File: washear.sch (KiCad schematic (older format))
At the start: 32 parts

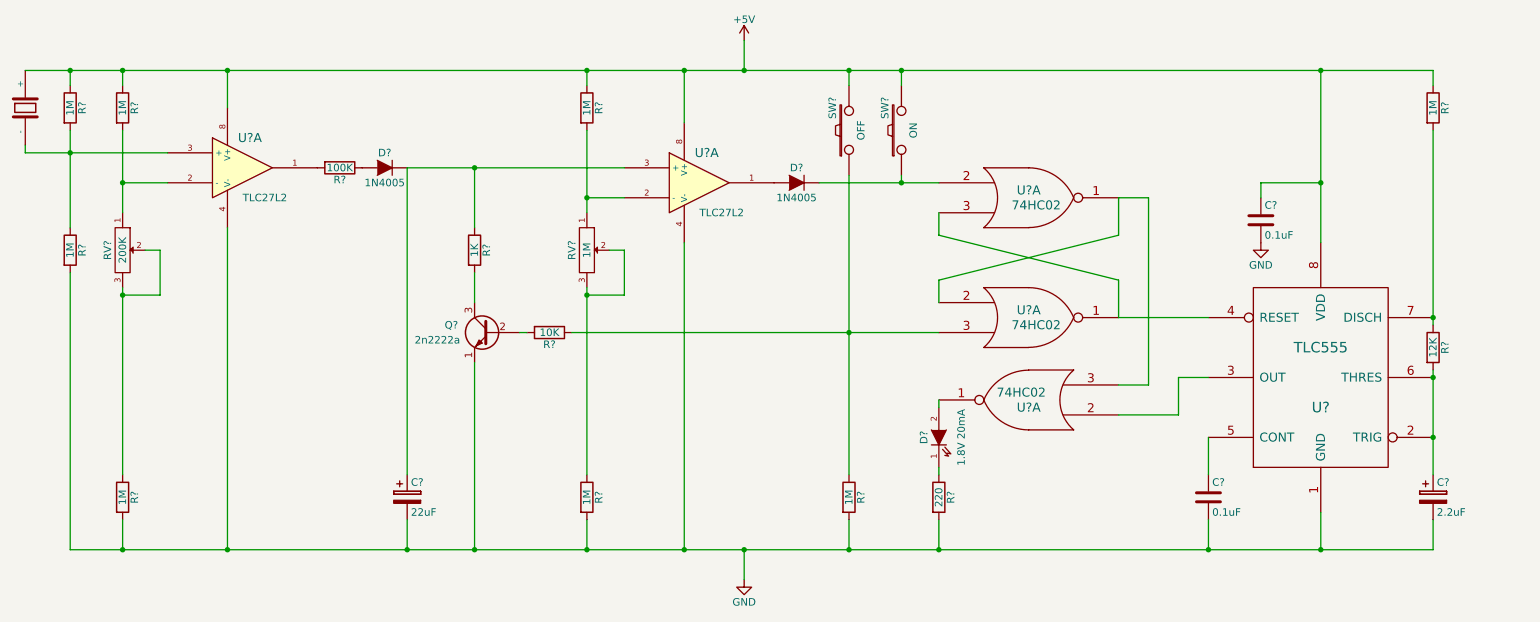
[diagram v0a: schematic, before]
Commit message: Power TLC555 from logic gate to save power
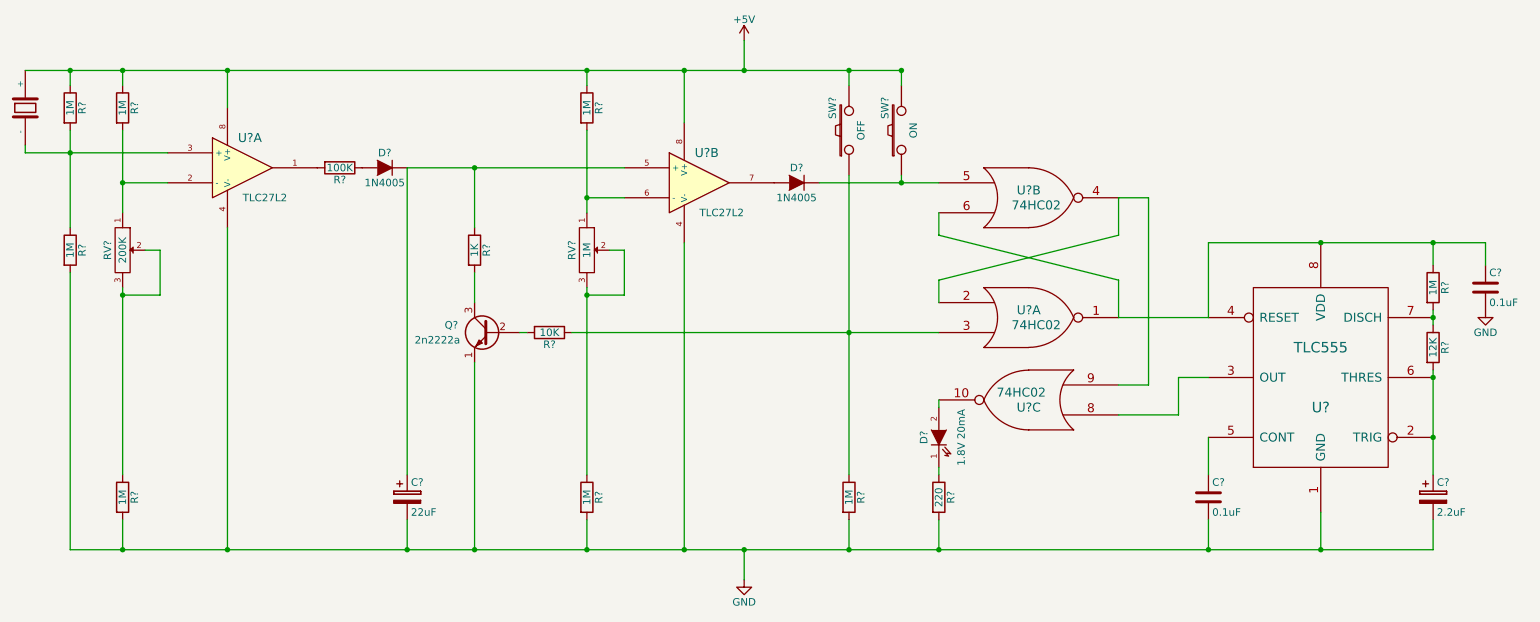
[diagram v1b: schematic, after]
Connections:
- net +5V: no longer C?.1, R?.1, U?.8 (VDD)
- net at U?.1, U?.4 (RESET): now also C?.1, R?.1, U?.6, U?.8 (VDD); no longer U?.3
- net at D?.1 (K), SW?.1: now also U?.5; no longer U?.2
- net at D?.2 (A): now also U?.7; no longer U?.1
- net at R?.2, RV?.1: now also U?.6 (-); no longer U?.2 (-)
- net at C?.1, D?.1 (K), R?.1: now also U?.5 (+); no longer U?.3 (+)
- net at D?.2 (A): now also U?.10; no longer U?.1
- net at U?.3 (OUT): now also U?.8; no longer U?.2
- new net: U?.2, U?.4, U?.9
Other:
- moved on the sheet: C?, R?
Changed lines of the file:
@@
 $Comp
 L 74HC02 U?
-U 1 1 55D4E108
+U 2 1 55D4E108
 P 7700 3250
 F 0 "U?" H 7700 3300 60  0000 C CNN
@@
 F 2 "~" H 7700 3250 60  0000 C CNN
 F 3 "~" H 7700 3250 60  0000 C CNN
-	1    7700 3250
+	2    7700 3250
 	1    0    0    -1
 $EndComp
@@
 $Comp
 L TLC27L2 U?
-U 1 1 55E35DBE
+U 2 1 55E35DBE
 P 5500 3150
 F 0 "U?" H 5550 3350 60  0000 C CNN
@@
 F 2 "" H 5500 3150 60  0000 C CNN
 F 3 "" H 5500 3150 60  0000 C CNN
-	1    5500 3150
+	2    5500 3150
 	1    0    0    -1
 $EndComp
@@
 Wire Wire Line
 	8300 3500 8300 3250
-Wire Wire Line
-	1000 2400 1300 2400
-Wire Wire Line
-	1300 2400 1650 2400
-Wire Wire Line
-	1650 2400 2350 2400
-Wire Wire Line
-	2350 2400 4750 2400
-Wire Wire Line
-	4750 2400 5400 2400
-Wire Wire Line
-	5400 2400 5800 2400
-Wire Wire Line
-	5800 2400 6500 2400
-Wire Wire Line
-	6500 2400 6850 2400
-Wire Wire Line
-	6850 2400 9650 2400
-Wire Wire Line
-	9650 2400 10400 2400
 Connection ~ 1650 5600
 Wire Wire Line
@@
 	9650 5600 10400 5600
 Connection ~ 8900 5600
-Wire Wire Line
-	9650 2400 9650 3150
-Wire Wire Line
-	9650 3150 9650 3550
 $Comp
 L R R?
 U 1 1 567C5142
-P 10400 2650
-F 0 "R?" V 10480 2650 50  0000 C CNN
-F 1 "1M" V 10400 2650 50  0000 C CNN
-F 2 "" V 10330 2650 30  0000 C CNN
-F 3 "" H 10400 2650 30  0000 C CNN
-	1    10400 2650
-	1    0    0    -1
-$EndComp
-Wire Wire Line
-	10400 2400 10400 2500
-Connection ~ 9650 2400
+P 10400 3850
+F 0 "R?" V 10480 3850 50  0000 C CNN
+F 1 "1M" V 10400 3850 50  0000 C CNN
+F 2 "" V 10330 3850 30  0000 C CNN
+F 3 "" H 10400 3850 30  0000 C CNN
+	1    10400 3850
+	1    0    0    -1
+$EndComp
 $Comp
 L R R?
@@
 $Comp
 L 74HC02 U?
-U 1 1 567C7051
+U 3 1 567C7051
 P 7700 4600
 F 0 "U?" H 7700 4650 60  0000 C CNN
@@
 F 2 "~" H 7700 4600 60  0000 C CNN
 F 3 "~" H 7700 4600 60  0000 C CNN
-	1    7700 4600
+	3    7700 4600
 	-1   0    0    1
 $EndComp
@@
 L C C?
 U 1 1 567ED50A
-P 9250 3400
-F 0 "C?" H 9275 3500 50  0000 L CNN
-F 1 "0.1uF" H 9275 3300 50  0000 L CNN
-F 2 "" H 9288 3250 30  0000 C CNN
-F 3 "" H 9250 3400 60  0000 C CNN
-	1    9250 3400
+P 10750 3850
+F 0 "C?" H 10775 3950 50  0000 L CNN
+F 1 "0.1uF" H 10775 3750 50  0000 L CNN
+F 2 "" H 10788 3700 30  0000 C CNN
+F 3 "" H 10750 3850 60  0000 C CNN
+	1    10750 3850
 	1    0    0    -1
 $EndComp
@@
 L GND #PWR?
 U 1 1 567ED5C0
-P 9250 3550
-F 0 "#PWR?" H 9250 3300 50  0001 C CNN
-F 1 "GND" H 9250 3400 50  0000 C CNN
-F 2 "" H 9250 3550 60  0000 C CNN
-F 3 "" H 9250 3550 60  0000 C CNN
-	1    9250 3550
-	1    0    0    -1
-$EndComp
-Wire Wire Line
-	9250 3150 9250 3250
+P 10750 4000
+F 0 "#PWR?" H 10750 3750 50  0001 C CNN
+F 1 "GND" H 10750 3850 50  0000 C CNN
+F 2 "" H 10750 4000 60  0000 C CNN
+F 3 "" H 10750 4000 60  0000 C CNN
+	1    10750 4000
+	1    0    0    -1
+$EndComp
 $Comp
 L D D?
@@
 	9650 5350 9650 5600
 Wire Wire Line
-	10400 2800 10400 4050
+	10400 4000 10400 4050
 Wire Wire Line
 	10400 4050 10400 4100
@@
 	1    0    0    -1
 $EndComp
-Wire Wire Line
-	9250 3150 9650 3150
-Connection ~ 9650 3150
 $Comp
 L TLC555 U?
@@
 	1    0    0    -1
 $EndComp
+Wire Wire Line
+	8900 4050 8900 3550
+Wire Wire Line
+	8900 3550 9650 3550
+Wire Wire Line
+	9650 3550 10400 3550
+Wire Wire Line
+	10400 3550 10750 3550
+Wire Wire Line
+	10400 3550 10400 3700
+Connection ~ 9650 3550
+Wire Wire Line
+	10750 3550 10750 3700
+Connection ~ 10400 3550
+Wire Wire Line
+	1000 2400 1300 2400
+Wire Wire Line
+	1300 2400 1650 2400
+Wire Wire Line
+	1650 2400 2350 2400
+Wire Wire Line
+	2350 2400 4750 2400
+Wire Wire Line
+	4750 2400 5400 2400
+Wire Wire Line
+	5400 2400 5800 2400
+Wire Wire Line
+	5800 2400 6500 2400
+Wire Wire Line
+	6500 2400 6850 2400
 $EndSCHEMATC

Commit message: Capture the final implemented schematic
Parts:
- RV1: renamed from RV?; value 200K -> 100K
- RV2: renamed from RV?; value 1M -> 500K
- gave numbers to parts that had none: 27
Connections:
- net at C4.1, R12.1, U3.4 (RESET)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: now also U2.3, U2.4; no longer U2.1, U2.6
- net at R10.1, R7.1, SW1.1: now also U2.6; no longer U2.3
- net at D2.1 (K), SW2.1: now also U2.2; no longer U2.5
- net at D3.2 (A): now also U2.13; no longer U2.10
- net at U3.3 (OUT): now also U2.11; no longer U2.8
- new net: U2.1, U2.12, U2.5
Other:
- moved on the sheet: C4
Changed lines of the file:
@@
 $EndDescr
 $Comp
-L PZ PZ?
+L PZ PZ1
 U 1 1 55D47824
 P 1000 2650
-F 0 "PZ?" H 1000 2780 40  0001 L CNN
+F 0 "PZ1" H 1000 2780 40  0001 L CNN
 F 1 "PZ" H 1006 2535 40  0001 L CNN
 F 2 "~" H 1038 2470 30  0000 C CNN
@@
 $EndComp
 $Comp
-L POT RV?
+L POT RV1
 U 1 1 55D4DDDE
 P 1650 3600
-F 0 "RV?" H 1650 3500 50  0000 C CNN
-F 1 "200K" H 1650 3600 50  0000 C CNN
+F 0 "RV1" H 1650 3500 50  0000 C CNN
+F 1 "100K" H 1650 3600 50  0000 C CNN
 F 2 "~" H 1650 3600 60  0000 C CNN
 F 3 "~" H 1650 3600 60  0000 C CNN
@@
 $EndComp
 $Comp
-L 74HC02 U?
-U 1 1 55D4DFF4
+L 74HC02 U2
+U 2 1 55D4DFF4
 P 7700 4050
-F 0 "U?" H 7700 4100 60  0000 C CNN
+F 0 "U2" H 7700 4100 60  0000 C CNN
 F 1 "74HC02" H 7750 4000 60  0000 C CNN
 F 2 "~" H 7700 4050 60  0000 C CNN
 F 3 "~" H 7700 4050 60  0000 C CNN
-	1    7700 4050
-	1    0    0    -1
-$EndComp
-$Comp
-L 74HC02 U?
-U 2 1 55D4E108
+	2    7700 4050
+	1    0    0    -1
+$EndComp
+$Comp
+L 74HC02 U2
+U 1 1 55D4E108
 P 7700 3250
-F 0 "U?" H 7700 3300 60  0000 C CNN
+F 0 "U2" H 7700 3300 60  0000 C CNN
 F 1 "74HC02" H 7750 3200 60  0000 C CNN
 F 2 "~" H 7700 3250 60  0000 C CNN
 F 3 "~" H 7700 3250 60  0000 C CNN
-	2    7700 3250
-	1    0    0    -1
-$EndComp
-$Comp
-L TLC27L2 U?
+	1    7700 3250
+	1    0    0    -1
+$EndComp
+$Comp
+L TLC27L2 U1
 U 1 1 55E34D0D
 P 2450 3050
-F 0 "U?" H 2500 3250 60  0000 C CNN
+F 0 "U1" H 2500 3250 60  0000 C CNN
 F 1 "TLC27L2" H 2600 2850 50  0000 C CNN
 F 2 "" H 2450 3050 60  0000 C CNN
@@
 $EndComp
 $Comp
-L TLC27L2 U?
+L TLC27L2 U1
 U 2 1 55E35DBE
 P 5500 3150
-F 0 "U?" H 5550 3350 60  0000 C CNN
+F 0 "U1" H 5550 3350 60  0000 C CNN
 F 1 "TLC27L2" H 5650 2950 50  0000 C CNN
 F 2 "" H 5500 3150 60  0000 C CNN
@@
 $EndComp
 $Comp
-L POT RV?
+L POT RV2
 U 1 1 55E35EEA
 P 4750 3600
-F 0 "RV?" H 4750 3500 50  0000 C CNN
-F 1 "1M" H 4750 3600 50  0000 C CNN
+F 0 "RV2" H 4750 3500 50  0000 C CNN
+F 1 "500K" H 4750 3600 50  0000 C CNN
 F 2 "~" H 4750 3600 60  0000 C CNN
 F 3 "~" H 4750 3600 60  0000 C CNN
@@
 $EndComp
 $Comp
-L SW_PUSH SW?
+L SW_PUSH SW1
 U 1 1 5627B2CF
 P 6500 2800
-F 0 "SW?" H 6650 2910 50  0000 C CNN
+F 0 "SW1" H 6650 2910 50  0000 C CNN
 F 1 "OFF" H 6500 2720 50  0000 C CNN
 F 2 "~" H 6500 2800 60  0000 C CNN
@@
 $EndComp
 $Comp
-L SW_PUSH SW?
+L SW_PUSH SW2
 U 1 1 5627B2DC
 P 6850 2800
-F 0 "SW?" H 7000 2910 50  0000 C CNN
+F 0 "SW2" H 7000 2910 50  0000 C CNN
 F 1 "ON" H 6850 2720 50  0000 C CNN
 F 2 "~" H 6850 2800 60  0000 C CNN
@@
 	7100 3800 8300 3500
 $Comp
-L C C?
+L C C2
 U 1 1 567C46A0
 P 8900 5250
-F 0 "C?" H 8925 5350 50  0000 L CNN
+F 0 "C2" H 8925 5350 50  0000 L CNN
 F 1 "0.1uF" H 8925 5150 50  0000 L CNN
 F 2 "" H 8938 5100 30  0000 C CNN
@@
 	8900 5600 8900 5400
 $Comp
-L R R?
+L R R13
 U 1 1 567C4B96
 P 10400 4250
-F 0 "R?" V 10480 4250 50  0000 C CNN
+F 0 "R13" V 10480 4250 50  0000 C CNN
 F 1 "12K" V 10400 4250 50  0000 C CNN
 F 2 "" V 10330 4250 30  0000 C CNN
@@
 $EndComp
 $Comp
-L CP C?
+L CP C3
 U 1 1 567C4E2B
 P 10400 5250
-F 0 "C?" H 10425 5350 50  0000 L CNN
+F 0 "C3" H 10425 5350 50  0000 L CNN
 F 1 "2.2uF" H 10425 5150 50  0000 L CNN
 F 2 "" H 10438 5100 30  0000 C CNN
@@
 Wire Wire Line
 	9650 5600 10400 5600
+Wire Wire Line
+	10400 5600 10750 5600
 Connection ~ 8900 5600
 $Comp
-L R R?
+L R R12
 U 1 1 567C5142
 P 10400 3850
-F 0 "R?" V 10480 3850 50  0000 C CNN
+F 0 "R12" V 10480 3850 50  0000 C CNN
 F 1 "1M" V 10400 3850 50  0000 C CNN
 F 2 "" V 10330 3850 30  0000 C CNN
@@
 $EndComp
 $Comp
-L R R?
+L R R8
 U 1 1 567C5369
 P 4750 2650
-F 0 "R?" V 4830 2650 50  0000 C CNN
+F 0 "R8" V 4830 2650 50  0000 C CNN
 F 1 "1M" V 4750 2650 50  0000 C CNN
 F 2 "" V 4680 2650 30  0000 C CNN
@@
 $EndComp
 Wire Wire Line
-	4750 2500 4750 2400
-$Comp
-L R R?
+	4750 2400 4750 2500
+$Comp
+L R R1
 U 1 1 567C567F
 P 1300 2650
-F 0 "R?" V 1380 2650 50  0000 C CNN
+F 0 "R1" V 1380 2650 50  0000 C CNN
 F 1 "1M" V 1300 2650 50  0000 C CNN
 F 2 "" V 1230 2650 30  0000 C CNN
@@
 $EndComp
 $Comp
-L R R?
+L R R3
 U 1 1 567C572F
 P 1650 2650
-F 0 "R?" V 1730 2650 50  0000 C CNN
+F 0 "R3" V 1730 2650 50  0000 C CNN
 F 1 "1M" V 1650 2650 50  0000 C CNN
 F 2 "" V 1580 2650 30  0000 C CNN
@@
 	1650 2400 1650 2500
 $Comp
-L R R?
+L R R2
 U 1 1 567C595D
 P 1300 3600
-F 0 "R?" V 1380 3600 50  0000 C CNN
+F 0 "R2" V 1380 3600 50  0000 C CNN
 F 1 "1M" V 1300 3600 50  0000 C CNN
 F 2 "" V 1230 3600 30  0000 C CNN
@@
 $EndComp
 $Comp
-L R R?
+L R R4
 U 1 1 567C5B76
 P 1650 5250
-F 0 "R?" V 1730 5250 50  0000 C CNN
+F 0 "R4" V 1730 5250 50  0000 C CNN
 F 1 "1M" V 1650 5250 50  0000 C CNN
 F 2 "" V 1580 5250 30  0000 C CNN
@@
 $EndComp
 $Comp
-L R R?
+L R R9
 U 1 1 567C5E2F
 P 4750 5250
-F 0 "R?" V 4830 5250 50  0000 C CNN
+F 0 "R9" V 4830 5250 50  0000 C CNN
 F 1 "1M" V 4750 5250 50  0000 C CNN
 F 2 "" V 4680 5250 30  0000 C CNN
@@
 $EndComp
 $Comp
-L R R?
+L R R10
 U 1 1 567C606F
 P 6500 5250
-F 0 "R?" V 6580 5250 50  0000 C CNN
+F 0 "R10" V 6580 5250 50  0000 C CNN
 F 1 "1M" V 6500 5250 50  0000 C CNN
 F 2 "" V 6430 5250 30  0000 C CNN
@@
 $EndComp
 $Comp
-L CP C?
+L CP C1
 U 1 1 567C65FE
 P 3550 5250
-F 0 "C?" H 3575 5350 50  0000 L CNN
+F 0 "C1" H 3575 5350 50  0000 L CNN
 F 1 "22uF" H 3575 5150 50  0000 L CNN
 F 2 "" H 3588 5100 30  0000 C CNN
@@
 $EndComp
 $Comp
-L R R?
+L R R5
 U 1 1 567C6977
 P 3100 3050
-F 0 "R?" V 3180 3050 50  0000 C CNN
+F 0 "R5" V 3180 3050 50  0000 C CNN
 F 1 "100K" V 3100 3050 50  0000 C CNN
 F 2 "" V 3030 3050 30  0000 C CNN
@@
 $EndComp
 $Comp
-L 74HC02 U?
-U 3 1 567C7051
+L 74HC02 U2
+U 4 1 567C7051
 P 7700 4600
-F 0 "U?" H 7700 4650 60  0000 C CNN
+F 0 "U2" H 7700 4650 60  0000 C CNN
 F 1 "74HC02" H 7750 4550 60  0000 C CNN
 F 2 "~" H 7700 4600 60  0000 C CNN
 F 3 "~" H 7700 4600 60  0000 C CNN
-	3    7700 4600
+	4    7700 4600
 	-1   0    0    1
 $EndComp
 $Comp
-L R R?
+L R R11
 U 1 1 567C750B
 P 7100 5250
-F 0 "R?" V 7180 5250 50  0000 C CNN
+F 0 "R11" V 7180 5250 50  0000 C CNN
 F 1 "220" V 7100 5250 50  0000 C CNN
 F 2 "" V 7030 5250 30  0000 C CNN
@@
 $EndComp
 $Comp
-L LED D?
+L LED D3
 U 1 1 567C7579
 P 7100 4850
-F 0 "D?" H 7100 4950 50  0000 C CNN
+F 0 "D3" H 7100 4950 50  0000 C CNN
 F 1 "1.8V 20mA" H 7100 4700 50  0000 C CNN
 F 2 "" H 7100 4850 60  0000 C CNN
@@
 Connection ~ 9650 5600
 Wire Wire Line
-	5800 2200 5800 2400
+	5800 2400 5800 2200
 Connection ~ 5800 2400
 $Comp
-L GND #PWR?
+L GND #PWR2
 U 1 1 567C092F
 P 5800 5800
-F 0 "#PWR?" H 5800 5550 50  0001 C CNN
+F 0 "#PWR2" H 5800 5550 50  0001 C CNN
 F 1 "GND" H 5800 5650 50  0000 C CNN
 F 2 "" H 5800 5800 60  0000 C CNN
@@
 Connection ~ 5800 5600
 $Comp
-L Q_NPN_EBC Q?
+L Q_NPN_EBC Q1
 U 1 1 567E961E
 P 4100 4150
-F 0 "Q?" H 4400 4200 50  0000 R CNN
+F 0 "Q1" H 4400 4200 50  0000 R CNN
 F 1 "2n2222a" H 4600 4100 50  0000 R CNN
 F 2 "" H 4300 4250 29  0000 C CNN
@@
 $EndComp
 $Comp
-L R R?
+L R R6
 U 1 1 567E98CB
 P 4000 3600
-F 0 "R?" V 4080 3600 50  0000 C CNN
+F 0 "R6" V 4080 3600 50  0000 C CNN
 F 1 "1K" V 4000 3600 50  0000 C CNN
 F 2 "" V 3930 3600 30  0000 C CNN
@@
 	4000 3750 4000 3950
 $Comp
-L D D?
+L D D1
 U 1 1 567E9AB2
 P 3400 3050
-F 0 "D?" H 3400 3150 50  0000 C CNN
+F 0 "D1" H 3400 3150 50  0000 C CNN
 F 1 "1N4005" H 3400 2950 50  0000 C CNN
 F 2 "" H 3400 3050 60  0000 C CNN
@@
 	5000 3900 4750 3900
 $Comp
-L R R?
+L R R7
 U 1 1 567EC382
 P 4500 4150
-F 0 "R?" V 4580 4150 50  0000 C CNN
+F 0 "R7" V 4580 4150 50  0000 C CNN
 F 1 "10K" V 4500 4150 50  0000 C CNN
 F 2 "" V 4430 4150 30  0000 C CNN
@@
 $EndComp
 $Comp
-L C C?
+L C C4
 U 1 1 567ED50A
-P 10750 3850
-F 0 "C?" H 10775 3950 50  0000 L CNN
-F 1 "0.1uF" H 10775 3750 50  0000 L CNN
-F 2 "" H 10788 3700 30  0000 C CNN
-F 3 "" H 10750 3850 60  0000 C CNN
-	1    10750 3850
-	1    0    0    -1
-$EndComp
-$Comp
-L GND #PWR?
-U 1 1 567ED5C0
-P 10750 4000
-F 0 "#PWR?" H 10750 3750 50  0001 C CNN
-F 1 "GND" H 10750 3850 50  0000 C CNN
-F 2 "" H 10750 4000 60  0000 C CNN
-F 3 "" H 10750 4000 60  0000 C CNN
-	1    10750 4000
-	1    0    0    -1
-$EndComp
-$Comp
-L D D?
+P 10750 5250
+F 0 "C4" H 10775 5350 50  0000 L CNN
+F 1 "0.1uF" H 10775 5150 50  0000 L CNN
+F 2 "" H 10788 5100 30  0000 C CNN
+F 3 "" H 10750 5250 60  0000 C CNN
+	1    10750 5250
+	1    0    0    -1
+$EndComp
+$Comp
+L D D2
 U 1 1 567EE47E
 P 6150 3150
-F 0 "D?" H 6150 3250 50  0000 C CNN
+F 0 "D2" H 6150 3250 50  0000 C CNN
 F 1 "1N4005" H 6150 3050 50  0000 C CNN
 F 2 "" H 6150 3150 60  0000 C CNN
@@
 Connection ~ 10400 4850
 $Comp
-L +5V #PWR?
+L +5V #PWR1
 U 1 1 567F81E2
 P 5800 2200
-F 0 "#PWR?" H 5800 2050 50  0001 C CNN
+F 0 "#PWR1" H 5800 2050 50  0001 C CNN
 F 1 "+5V" H 5800 2340 50  0000 C CNN
 F 2 "" H 5800 2200 60  0000 C CNN
@@
 $EndComp
 $Comp
-L TLC555 U?
+L TLC555 U3
 U 1 1 567F963C
 P 9650 4450
-F 0 "U?" H 9650 4250 70  0000 C CNN
+F 0 "U3" H 9650 4250 70  0000 C CNN
 F 1 "TLC555" H 9650 4650 70  0000 C CNN
 F 2 "" H 9650 4450 60  0000 C CNN
@@
 Connection ~ 9650 3550
 Wire Wire Line
-	10750 3550 10750 3700
+	10750 3550 10750 5100
 Connection ~ 10400 3550
 Wire Wire Line
@@
 Wire Wire Line
 	6500 2400 6850 2400
+Wire Wire Line
+	10750 5600 10750 5400
+Connection ~ 10400 5600
 $EndSCHEMATC
